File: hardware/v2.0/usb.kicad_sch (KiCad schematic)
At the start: 48 parts, among them J3 USB_C_Receptacle_USB2.0_14P, J4 USB_C_Receptacle_USB2.0_14P, J5 USB_C_Receptacle_USB2.0_14P, U1 ECP5U-25F-CABGA256, U10 TPD2EUSB30A, U7 TPD2EUSB30A, U8 TPD2EUSB30A, U9 FT231XQ

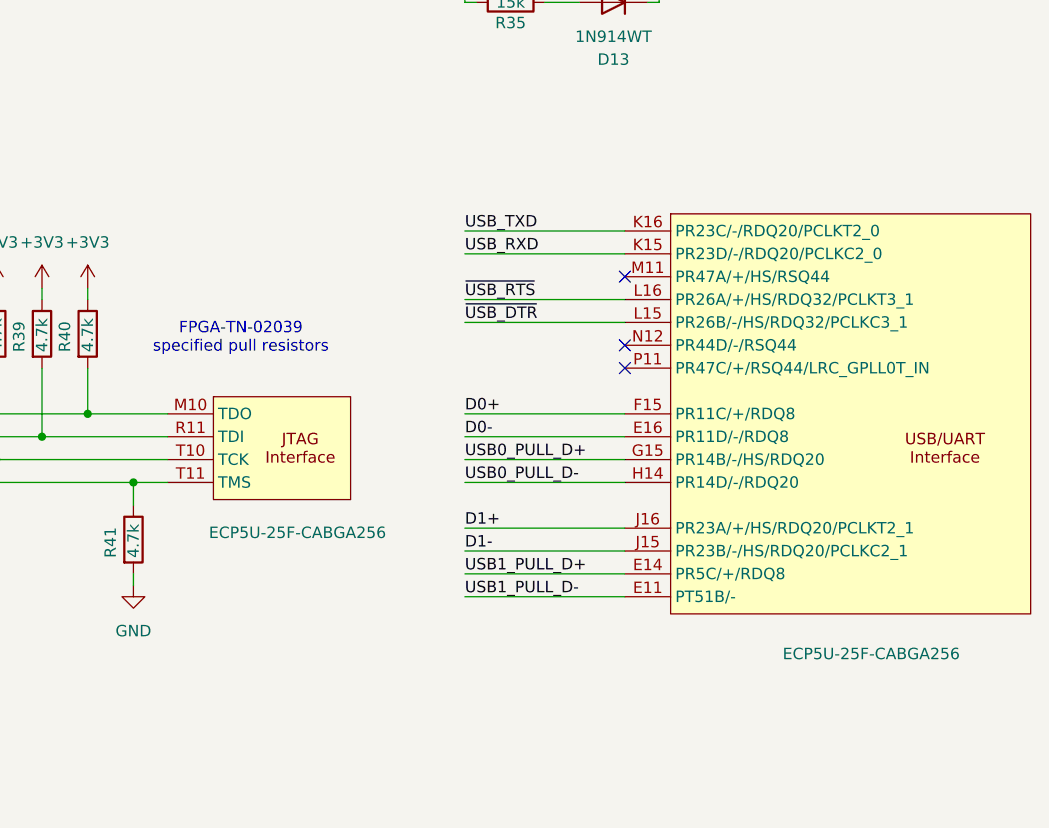
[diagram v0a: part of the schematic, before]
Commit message: ADC 6 diff lines
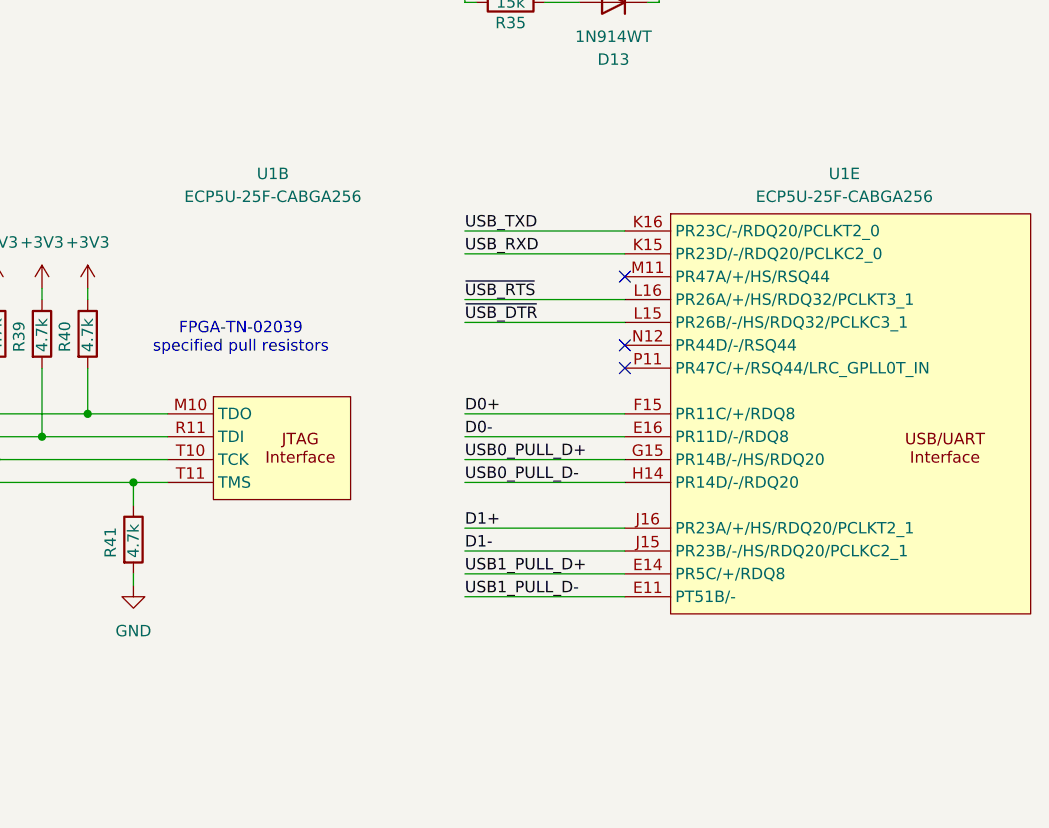
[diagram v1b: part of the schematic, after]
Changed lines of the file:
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@@
 		(dnp no)
 		(property "Reference" "U1"
-			(at 196.342 64.262 0)
+			(at 197.104 101.6 0)
 			(effects
 				(font
 					(size 1.27 1.27)
 				)
-				(hide yes)
 			)
 		)
 		(property "Value" "ECP5U-25F-CABGA256"
-			(at 189.992 141.478 0)
+			(at 197.104 104.14 0)
 			(effects
 				(font
 					(size 1.27 1.27)
 				)
-				(justify left)
 			)
 		)
@@
 					(unit 2)
 				)
+				(path "/f88da08e-cf42-4d03-a08f-3f602fe6658d/b5a9aa02-311b-4a9a-a7d4-646f15cdd9c2"
+					(reference "U1")
+					(unit 2)
+				)
 				(path "/f88da08e-cf42-4d03-a08f-3f602fe6658d/b8c813e2-b0ac-42df-b4a2-893985a7d29c"
 					(reference "U1")
@@
 		(dnp no)
 		(property "Reference" "U1"
-			(at 259.842 64.262 0)
+			(at 260.604 101.6 0)
 			(effects
 				(font
 					(size 1.27 1.27)
 				)
-				(hide yes)
 			)
 		)
 		(property "Value" "ECP5U-25F-CABGA256"
-			(at 253.746 154.94 0)
+			(at 260.604 104.14 0)
 			(effects
 				(font
 					(size 1.27 1.27)
 				)
-				(justify left)
 			)
 		)
@@
 					(reference "U1")
 					(unit 5)
+				)
+				(path "/f88da08e-cf42-4d03-a08f-3f602fe6658d/b5a9aa02-311b-4a9a-a7d4-646f15cdd9c2"
+					(reference "U1")
+					(unit 5)

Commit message: ADC CLKOUT±
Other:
- company: Chengyin Yao (cheyao), Vadym Vikulin -> Vadym Vikulin, Chengyin Yao (cheyao)
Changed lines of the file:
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@@
 	(title_block
 		(title "Icepi Zero")
-		(date "2026-01-05")
-		(rev "v2.0")
-		(company "Chengyin Yao (cheyao), Vadym Vikulin")
-		(comment 1 "https://github.com/cheyao/icepi-zero")
+		(date "2026-01-17")
+		(rev "v2.1")
+		(company "Vadym Vikulin, Chengyin Yao (cheyao)")
+		(comment 1 "https://github.com/vikulin/icepi-zero")
 		(comment 2 "License: Solderpad")
 		(comment 9 "OSHWA FR000026")
@@
 		(pin "P11"
 		)
+		(pin "N6"
+		)
 		(instances
 			(project ""
@@
 		(pin "F8"
 		)
+		(pin "N6"
+		)
 		(instances

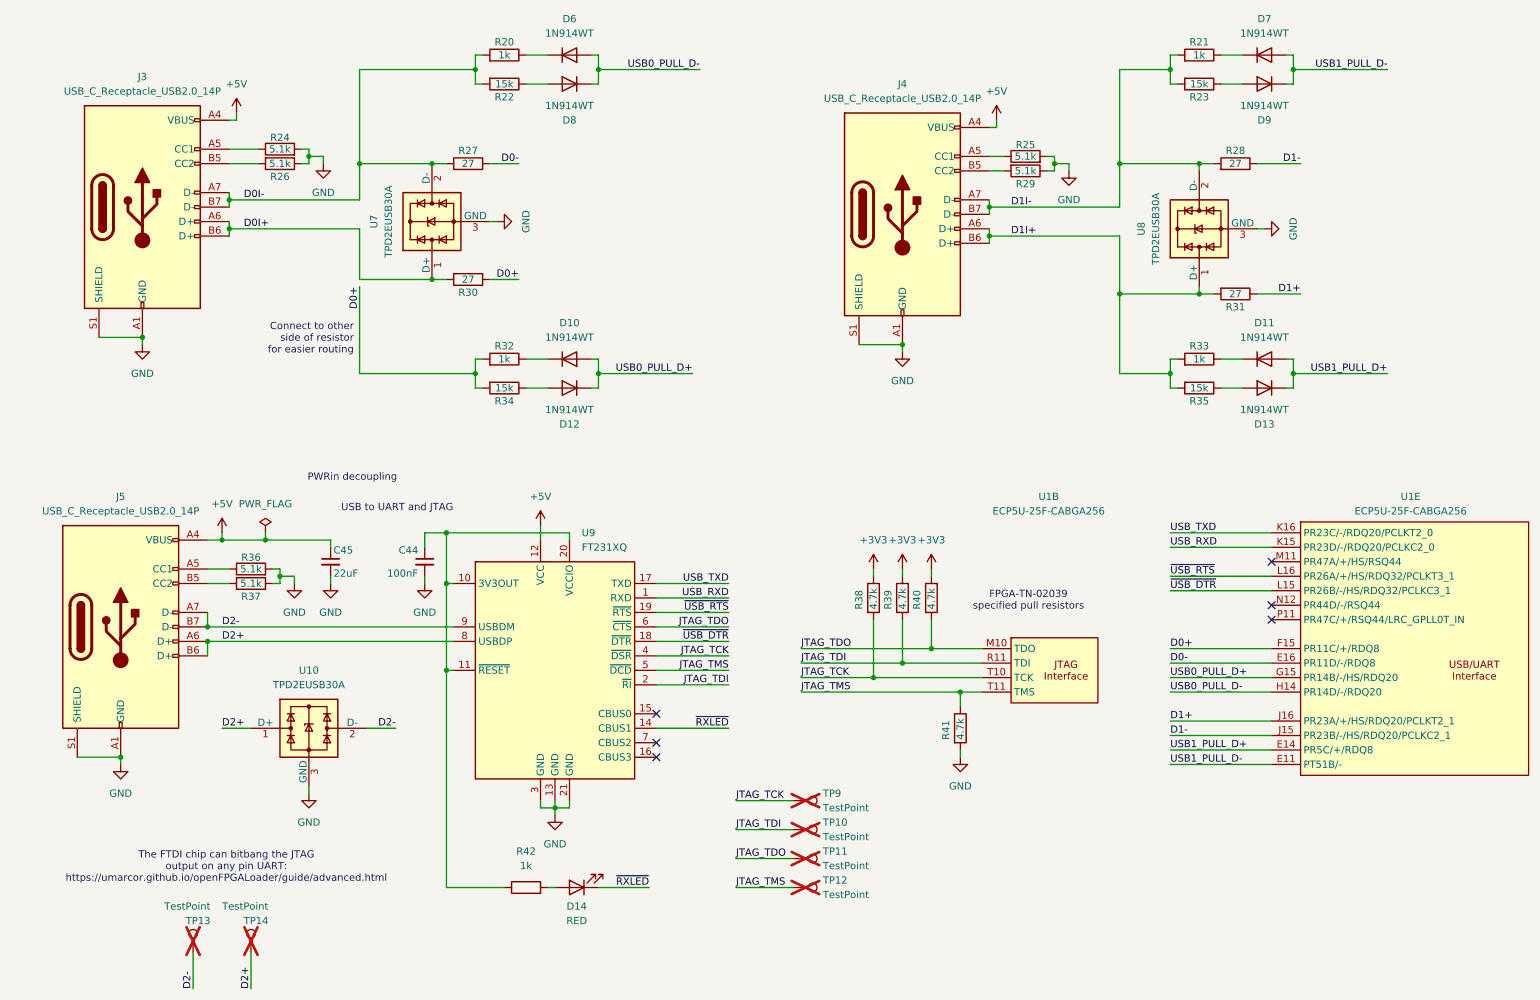
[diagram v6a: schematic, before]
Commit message: BOM fields unification for PCBWay requirements
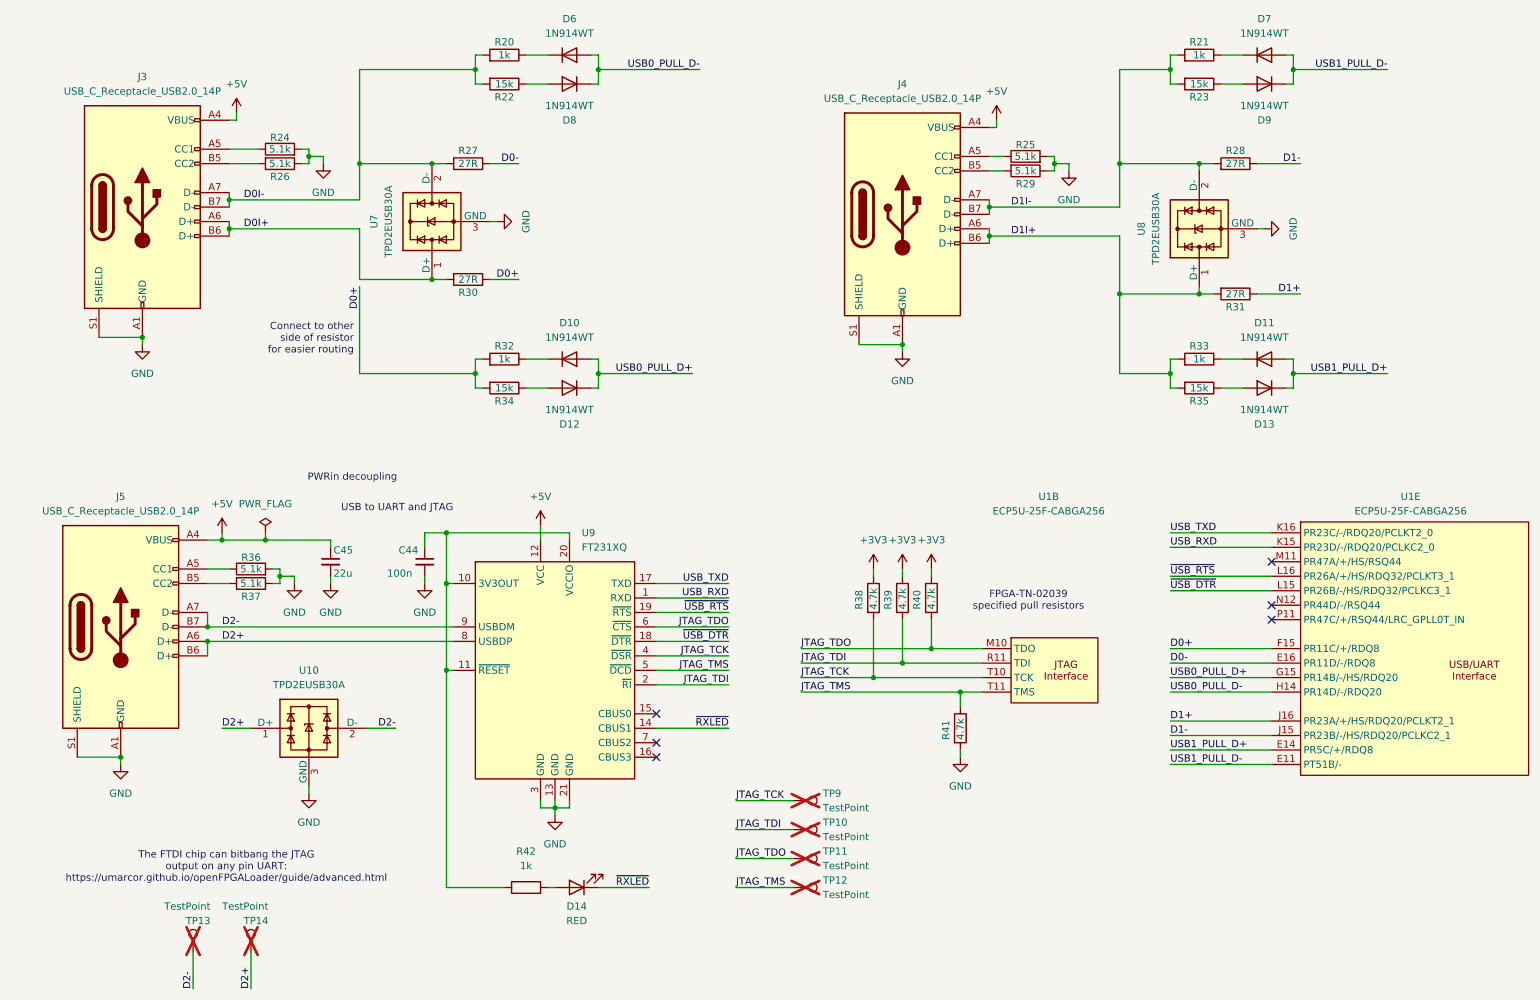
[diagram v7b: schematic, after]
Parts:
- C44: value 100nF -> 100n; MANUFACTURER (none) -> Samsung Electro-Mechanics; MANUFACTURER_PART_NUMBER (none) -> CL05B104KB54PNC
- C45: value 22uF -> 22u; MANUFACTURER (none) -> Samsung Electro-Mechanics; MANUFACTURER_PART_NUMBER (none) -> CL10A226MQ8NRNC
- D10, D11, D12, D13, D6, D7, D8, D9: MANUFACTURER (none) -> CBI; MANUFACTURER_PART_NUMBER (none) -> 1N914WT
- D14: MANUFACTURER (none) -> Hubei KENTO Elec; MANUFACTURER_PART_NUMBER (none) -> KT-0603R
- J3, J4, J5: MANUFACTURER (none) -> SHOU HAN; MANUFACTURER_PART_NUMBER (none) -> TYPE-C 16PIN 2MD(073)
- R20, R21, R32, R33, R42: MANUFACTURER (none) -> UNI-ROYAL; MANUFACTURER_PART_NUMBER (none) -> 0402WGF1001TCE
- R22, R23, R34, R35: MANUFACTURER (none) -> UNI-ROYAL; MANUFACTURER_PART_NUMBER (none) -> 0402WGF1502TCE
- R24, R25, R26, R29, R36, R37: MANUFACTURER (none) -> UNI-ROYAL; MANUFACTURER_PART_NUMBER (none) -> 0402WGF5101TCE
- R27, R28, R30, R31: value 27 -> 27R; MANUFACTURER (none) -> UNI-ROYAL; MANUFACTURER_PART_NUMBER (none) -> 0201WMF270JTEE
- R38, R39, R40, R41: MANUFACTURER (none) -> UNI-ROYAL; MANUFACTURER_PART_NUMBER (none) -> 0402WGF4701TCE
- U1: MANUFACTURER (none) -> Lattice; MANUFACTURER_PART_NUMBER (none) -> LFE5U-25F-6BG256C
- U10, U7, U8: MANUFACTURER (none) -> TECH PUBLIC; MANUFACTURER_PART_NUMBER (none) -> TPD2EUSB30ADRTR
- U9: MANUFACTURER (none) -> FTDI; MANUFACTURER_PART_NUMBER (none) -> FT231XQ-R
